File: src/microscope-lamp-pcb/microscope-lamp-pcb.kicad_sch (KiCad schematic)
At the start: 28 parts, among them J1 USB_C_Receptacle_PowerOnly_6P, U1 AP5724WG

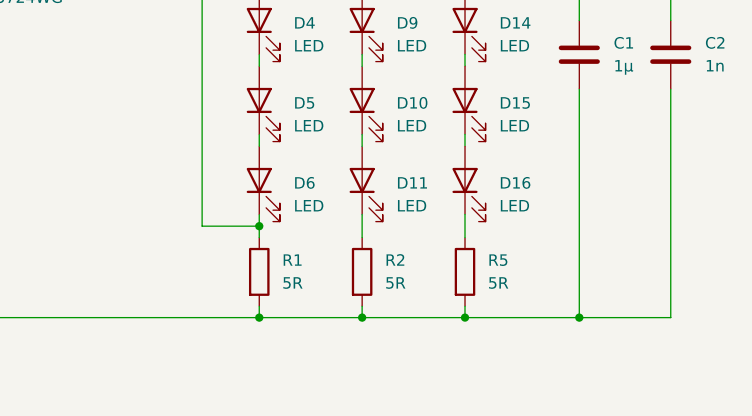
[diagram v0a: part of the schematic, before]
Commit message: Updating component info.
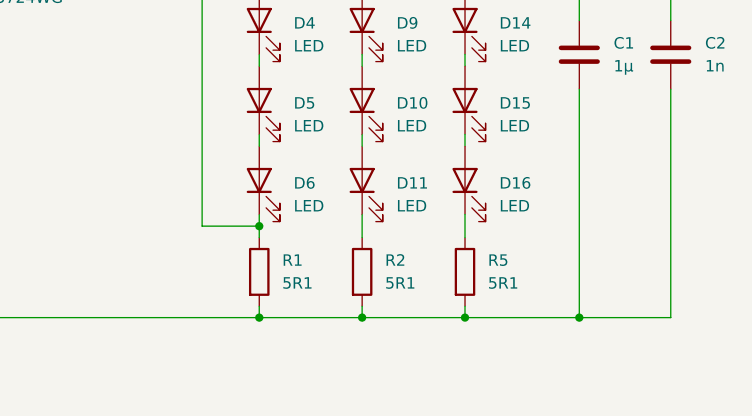
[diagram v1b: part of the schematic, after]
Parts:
- C1, C3: MF ID: (none) -> CL10A105KO8NNNC; MF: (none) -> SAMSUNG; TME ID: (none) -> CL10A105KO8NNNC; TME LINK: (none) -> https://www.tme.eu/pl/details/cl10a105ko8nnnc/kondensatory-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
- C2, C4: MF ID: (none) -> CL10B102KB8WPNC; MF: (none) -> SAMSUNG; TME ID: (none) -> CL10B102KB8WPNC; TME LINK: (none) -> https://www.tme.eu/pl/details/cl10b102kb8wpnc/kondensatory-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
- R1, R2, R5: value 5R -> 5R1; MF ID: (none) -> AC0603FR-075R1L; MF: (none) -> YAGEO; TME ID: (none) -> AC0603FR-075R1L; TME LINK: (none) -> https://www.tme.eu/pl/details/ac0603fr-075r1l/rezystory-smd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
- R3, R4: MF ID: (none) -> AC0603FR-075K1L; MF: (none) -> YAGEO; TME ID: (none) -> AC0603FR-075K1L; TME LINK: (none) -> https://www.tme.eu/pl/details/ac0603fr-075k1l/rezystory-smd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
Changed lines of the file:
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@@
+      (effects (font (size 1.27 1.27)) hide)
+    )
+    (property "MF ID:" "AC0603FR-075K1L" (at 101.6 102.87 0)
+      (effects (font (size 1.27 1.27)) hide)
+    )
+    (property "MF:" "YAGEO" (at 101.6 102.87 0)
+      (effects (font (size 1.27 1.27)) hide)
+    )
+    (property "TME ID:" "AC0603FR-075K1L" (at 101.6 102.87 0)
+      (effects (font (size 1.27 1.27)) hide)
+    )
+    (property "TME LINK:" "https://www.tme.eu/pl/details/ac0603fr-075k1l/rezystory-smd/yageo/" (at 101.6 102.87 0)
       (effects (font (size 1.27 1.27)) hide)
     )
@@
     )
     (property "Datasheet" "~" (at 220.98 95.25 0)
+      (effects (font (size 1.27 1.27)) hide)
+    )
+    (property "MF ID:" "CL10B102KB8WPNC" (at 220.98 95.25 0)
+      (effects (font (size 1.27 1.27)) hide)
+    )
+    (property "MF:" "SAMSUNG" (at 220.98 95.25 0)
+      (effects (font (size 1.27 1.27)) hide)
+    )
+    (property "TME ID:" "CL10B102KB8WPNC" (at 220.98 95.25 0)
+      (effects (font (size 1.27 1.27)) hide)
+    )
+    (property "TME LINK:" "https://www.tme.eu/pl/details/cl10b102kb8wpnc/kondensatory-mlcc-smd/samsung/" (at 220.98 95.25 0)
       (effects (font (size 1.27 1.27)) hide)
     )
@@
       (effects (font (size 1.27 1.27)) hide)
     )
+    (property "MF ID:" "CL10B102KB8WPNC" (at 127 73.66 0)
+      (effects (font (size 1.27 1.27)) hide)
+    )
+    (property "MF:" "SAMSUNG" (at 127 73.66 0)
+      (effects (font (size 1.27 1.27)) hide)
+    )
+    (property "TME ID:" "CL10B102KB8WPNC" (at 127 73.66 0)
+      (effects (font (size 1.27 1.27)) hide)
+    )
+    (property "TME LINK:" "https://www.tme.eu/pl/details/cl10b102kb8wpnc/kondensatory-mlcc-smd/samsung/" (at 127 73.66 0)
+      (effects (font (size 1.27 1.27)) hide)
+    )
     (pin "1")
     (pin "2")
@@
       (effects (font (size 1.27 1.27)) (justify left))
     )
-    (property "Value" "5R" (at 200.66 120.65 0)
+    (property "Value" "5R1" (at 200.66 120.65 0)
       (effects (font (size 1.27 1.27)) (justify left))
     )
@@
       (effects (font (size 1.27 1.27)) hide)
     )
+    (property "MF ID:" "AC0603FR-075R1L" (at 198.12 119.38 0)
+      (effects (font (size 1.27 1.27)) hide)
+    )
+    (property "MF:" "YAGEO" (at 198.12 119.38 0)
+      (effects (font (size 1.27 1.27)) hide)
+    )
+    (property "TME ID:" "AC0603FR-075R1L" (at 198.12 119.38 0)
+      (effects (font (size 1.27 1.27)) hide)
+    )
+    (property "TME LINK:" "https://www.tme.eu/pl/details/ac0603fr-075r1l/rezystory-smd/yageo/" (at 198.12 119.38 0)
+      (effects (font (size 1.27 1.27)) hide)
+    )
     (pin "1")
     (pin "2")
@@
       (effects (font (size 1.27 1.27)) hide)
     )
+    (property "MF ID:" "AC0603FR-075K1L" (at 109.22 102.87 0)
+      (effects (font (size 1.27 1.27)) hide)
+    )
+    (property "MF:" "YAGEO" (at 109.22 102.87 0)
+      (effects (font (size 1.27 1.27)) hide)
+    )
+    (property "TME ID:" "AC0603FR-075K1L" (at 109.22 102.87 0)
+      (effects (font (size 1.27 1.27)) hide)
+    )
+    (property "TME LINK:" "https://www.tme.eu/pl/details/ac0603fr-075k1l/rezystory-smd/yageo/" (at 109.22 102.87 0)
+      (effects (font (size 1.27 1.27)) hide)
+    )
     (pin "1")
     (pin "2")
@@
       (effects (font (size 1.27 1.27)) hide)
     )
+    (property "MF ID:" "CL10A105KO8NNNC" (at 116.84 73.66 0)
+      (effects (font (size 1.27 1.27)) hide)
+    )
+    (property "MF:" "SAMSUNG" (at 116.84 73.66 0)
+      (effects (font (size 1.27 1.27)) hide)
+    )
+    (property "TME ID:" "CL10A105KO8NNNC" (at 116.84 73.66 0)
+      (effects (font (size 1.27 1.27)) hide)
+    )
+    (property "TME LINK:" "https://www.tme.eu/pl/details/cl10a105ko8nnnc/kondensatory-mlcc-smd/samsung/" (at 116.84 73.66 0)
+      (effects (font (size 1.27 1.27)) hide)
+    )
     (pin "1")
     (pin "2")
@@
       (effects (font (size 1.27 1.27)) (justify left))
     )
-    (property "Value" "5R" (at 189.23 120.65 0)
+    (property "Value" "5R1" (at 189.23 120.65 0)
       (effects (font (size 1.27 1.27)) (justify left))
     )
@@
     )
     (property "Datasheet" "~" (at 186.69 119.38 0)
+      (effects (font (size 1.27 1.27)) hide)
+    )
+    (property "MF ID:" "AC0603FR-075R1L" (at 186.69 119.38 0)
+      (effects (font (size 1.27 1.27)) hide)
+    )
+    (property "MF:" "YAGEO" (at 186.69 119.38 0)
+      (effects (font (size 1.27 1.27)) hide)
+    )
+    (property "TME ID:" "AC0603FR-075R1L" (at 186.69 119.38 0)
+      (effects (font (size 1.27 1.27)) hide)
+    )
+    (property "TME LINK:" "https://www.tme.eu/pl/details/ac0603fr-075r1l/rezystory-smd/yageo/" (at 186.69 119.38 0)
       (effects (font (size 1.27 1.27)) hide)
     )
@@
       (effects (font (size 1.27 1.27)) hide)
     )
+    (property "MF ID:" "CL10A105KO8NNNC" (at 210.82 95.25 0)
+      (effects (font (size 1.27 1.27)) hide)
+    )
+    (property "MF:" "SAMSUNG" (at 210.82 95.25 0)
+      (effects (font (size 1.27 1.27)) hide)
+    )
+    (property "TME ID:" "CL10A105KO8NNNC" (at 210.82 95.25 0)
+      (effects (font (size 1.27 1.27)) hide)
+    )
+    (property "TME LINK:" "https://www.tme.eu/pl/details/cl10a105ko8nnnc/kondensatory-mlcc-smd/samsung/" (at 210.82 95.25 0)
+      (effects (font (size 1.27 1.27)) hide)
+    )
     (pin "1")
     (pin "2")
@@
       (effects (font (size 1.27 1.27)) (justify left))
     )
-    (property "Value" "5R" (at 177.8 120.65 0)
+    (property "Value" "5R1" (at 177.8 120.65 0)
       (effects (font (size 1.27 1.27)) (justify left))
     )
@@
       (effects (font (size 1.27 1.27)) hide)
     )
+    (property "MF ID:" "AC0603FR-075R1L" (at 175.26 119.38 0)
+      (effects (font (size 1.27 1.27)) hide)
+    )
+    (property "MF:" "YAGEO" (at 175.26 119.38 0)
+      (effects (font (size 1.27 1.27)) hide)
+    )
+    (property "TME ID:" "AC0603FR-075R1L" (at 175.26 119.38 0)
+      (effects (font (size 1.27 1.27)) hide)
+    )
+    (property "TME LINK:" "https://www.tme.eu/pl/details/ac0603fr-075r1l/rezystory-smd/yageo/" (at 175.26 119.38 0)
+      (effects (font (size 1.27 1.27)) hide)
+    )
